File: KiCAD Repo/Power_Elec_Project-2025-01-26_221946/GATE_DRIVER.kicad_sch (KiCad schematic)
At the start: 0 parts

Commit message: lpf design
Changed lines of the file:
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@@
 	(hierarchical_label "VG"
 		(shape output)
-		(at 191.77 29.21 0)
+		(at 190.5 29.21 0)
 		(effects
 			(font

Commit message: gate driver import
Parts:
- added U3: ~, UCC5304DWVR GateDriver_IC:SOIC8_DWV_TEX, symbol UCC5304DWVR:UCC5304DWVR
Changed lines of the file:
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@@
 	(generator_version "8.0")
 	(paper "A4")
+	(wire
+		(pts
+			(xy 93.98 55.88) (xy 93.98 54.61)
+		)
+		(stroke
+			(width 0)
+			(type default)
+		)
+	)
+	(wire
+		(pts
+			(xy 92.71 55.88) (xy 93.98 55.88)
+		)
+		(stroke
+			(width 0)
+			(type default)
+		)
+	)
 	(hierarchical_label "VSW"
 		(shape output)
@@
 	(hierarchical_label "PWM"
 		(shape input)
-		(at 120.65 33.02 0)
-		(effects
-			(font
-				(size 1.27 1.27)
-			)
-			(justify left)
+		(at 92.71 58.42 180)
+		(effects
+			(font
+				(size 1.27 1.27)
+			)
+			(justify right)
 		)
 	)
 	(hierarchical_label "GND"
 		(shape input)
-		(at 120.65 40.64 0)
-		(effects
-			(font
-				(size 1.27 1.27)
-			)
-			(justify left)
+		(at 92.71 60.96 180)
+		(effects
+			(font
+				(size 1.27 1.27)
+			)
+			(justify right)
 		)
 	)
 	(hierarchical_label "5V"
 		(shape input)
-		(at 120.65 26.67 0)
-		(effects
-			(font
-				(size 1.27 1.27)
-			)
-			(justify left)
+		(at 92.71 55.88 180)
+		(effects
+			(font
+				(size 1.27 1.27)
+			)
+			(justify right)
 		)
 	)
@@
 		)
 	)
+	(symbol
+		(lib_id "UCC5304DWVR:UCC5304DWVR")
+		(at 101.6 55.88 0)
+		(unit 1)
+		(exclude_from_sim no)
+		(in_bom yes)
+		(on_board yes)
+		(dnp no)
+		(property "Reference" "U3"
+			(at 110.998 49.276 0)
+			(effects
+				(font
+					(size 1.524 1.524)
+				)
+			)
+		)
+		(property "Value" "~"
+			(at 121.92 48.26 0)
+			(effects
+				(font
+					(size 1.524 1.524)
+				)
+				(hide yes)
+			)
+		)
+		(property "Footprint" "UCC5304DWVR GateDriver_IC:SOIC8_DWV_TEX"
+			(at 101.6 55.88 0)
+			(effects
+				(font
+					(size 1.27 1.27)
+					(italic yes)
+				)
+				(hide yes)
+			)
+		)
+		(property "Datasheet" "https://www.ti.com/lit/ds/symlink/ucc5304.pdf?ts=1739952660041&ref_url=https%253A%252F%252Fwww.mouser.de%252F"
+			(at 101.6 55.88 0)
+			(effects
+				(font
+					(size 1.27 1.27)
+					(italic yes)
+				)
+				(hide yes)
+			)
+		)
+		(property "Description" ""
+			(at 101.6 55.88 0)
+			(effects
+				(font
+					(size 1.27 1.27)
+				)
+				(hide yes)
+			)
+		)
+		(property "Part Number" "UCC5304DWVR"
+			(at 122.428 70.104 0)
+			(effects
+				(font
+					(size 1.27 1.27)
+				)
+			)
+		)
+		(pin "2"
+		)
+		(pin "7"
+		)
+		(pin "5"
+		)
+		(pin "1"
+		)
+		(pin "4"
+		)
+		(pin "6"
+		)
+		(pin "8"
+		)
+		(pin "3"
+		)
+		(instances
+			(project ""
+				(path "/ecd51ed2-b30f-41c1-93fa-3d04786e684e/43f1fb70-bf5d-401c-a26b-88dd12fd13e5"
+					(reference "U3")
+					(unit 1)
+				)
+			)
+		)
+	)
+	(symbol
+		(lib_id "power:+5V")
+		(at 93.98 54.61 0)
+		(unit 1)
+		(exclude_from_sim no)
+		(in_bom yes)
+		(on_board yes)
+		(dnp no)
+		(fields_autoplaced yes)
+		(property "Reference" "#PWR015"
+			(at 93.98 58.42 0)
+			(effects
+				(font
+					(size 1.27 1.27)
+				)
+				(hide yes)
+			)
+		)
+		(property "Value" "+5V"
+			(at 93.98 49.53 0)
+			(effects
+				(font
+					(size 1.27 1.27)
+				)
+			)
+		)
+		(property "Footprint" ""
+			(at 93.98 54.61 0)
+			(effects
+				(font
+					(size 1.27 1.27)
+				)
+				(hide yes)
+			)
+		)
+		(property "Datasheet" ""
+			(at 93.98 54.61 0)
+			(effects
+				(font
+					(size 1.27 1.27)
+				)
+				(hide yes)
+			)
+		)
+		(property "Description" "Power symbol creates a global label with name \"+5V\""
+			(at 93.98 54.61 0)
+			(effects
+				(font
+					(size 1.27 1.27)
+				)
+				(hide yes)
+			)
+		)
+		(pin "1"
+		)
+		(instances
+			(project ""
+				(path "/ecd51ed2-b30f-41c1-93fa-3d04786e684e/43f1fb70-bf5d-401c-a26b-88dd12fd13e5"
+					(reference "#PWR015")
+					(unit 1)
+				)
+			)
+		)
+	)

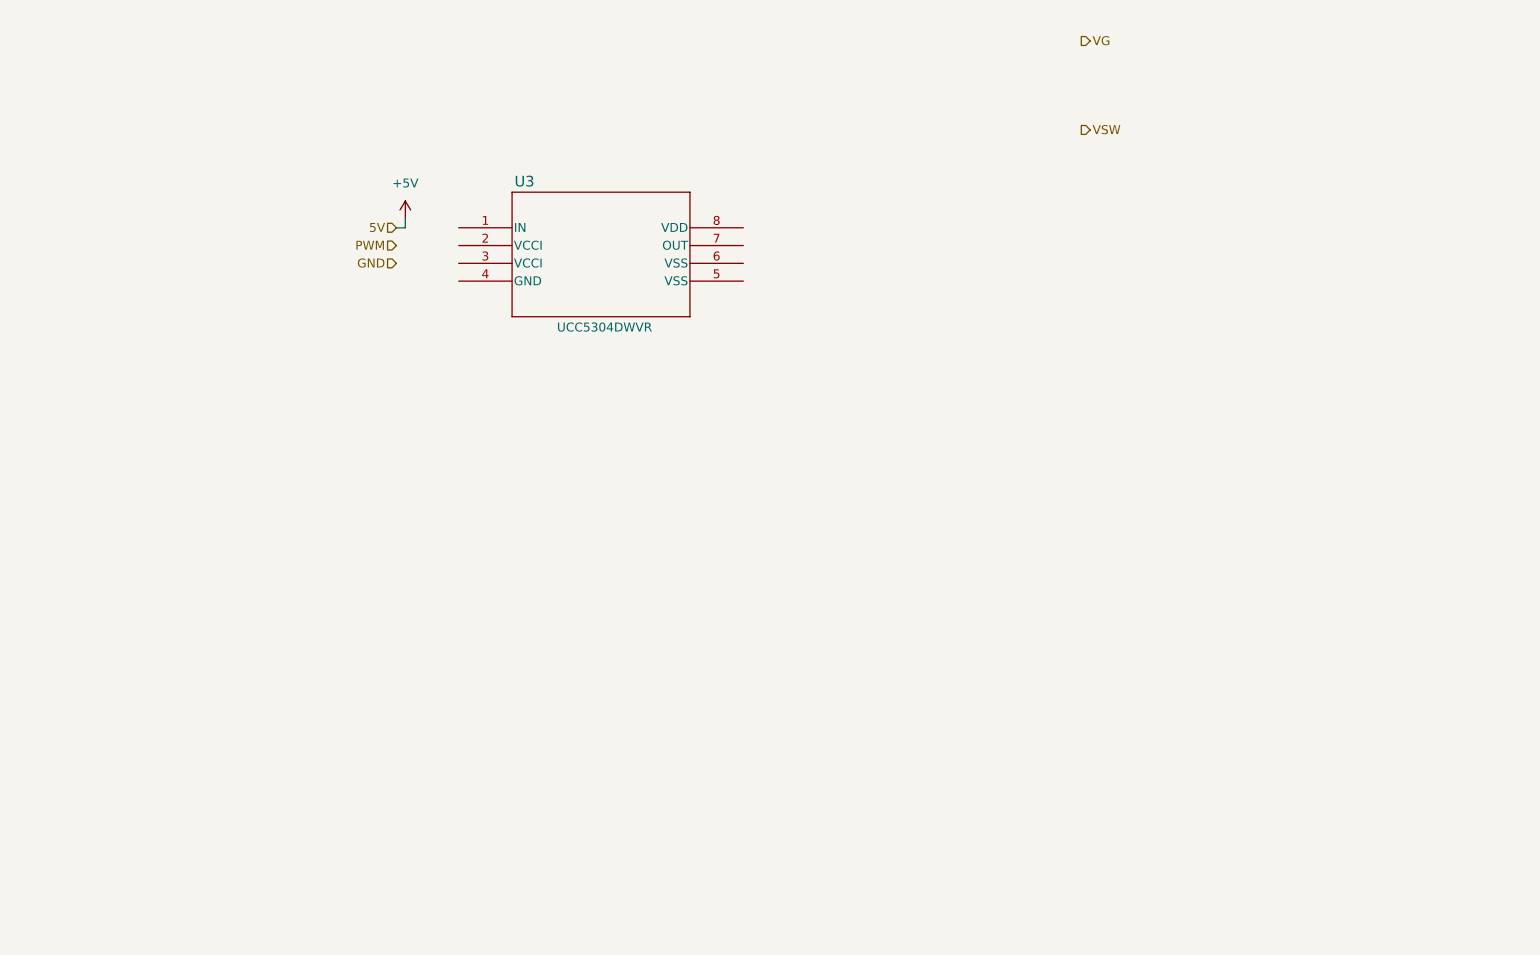
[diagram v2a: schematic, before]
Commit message: PLF and GD circuit
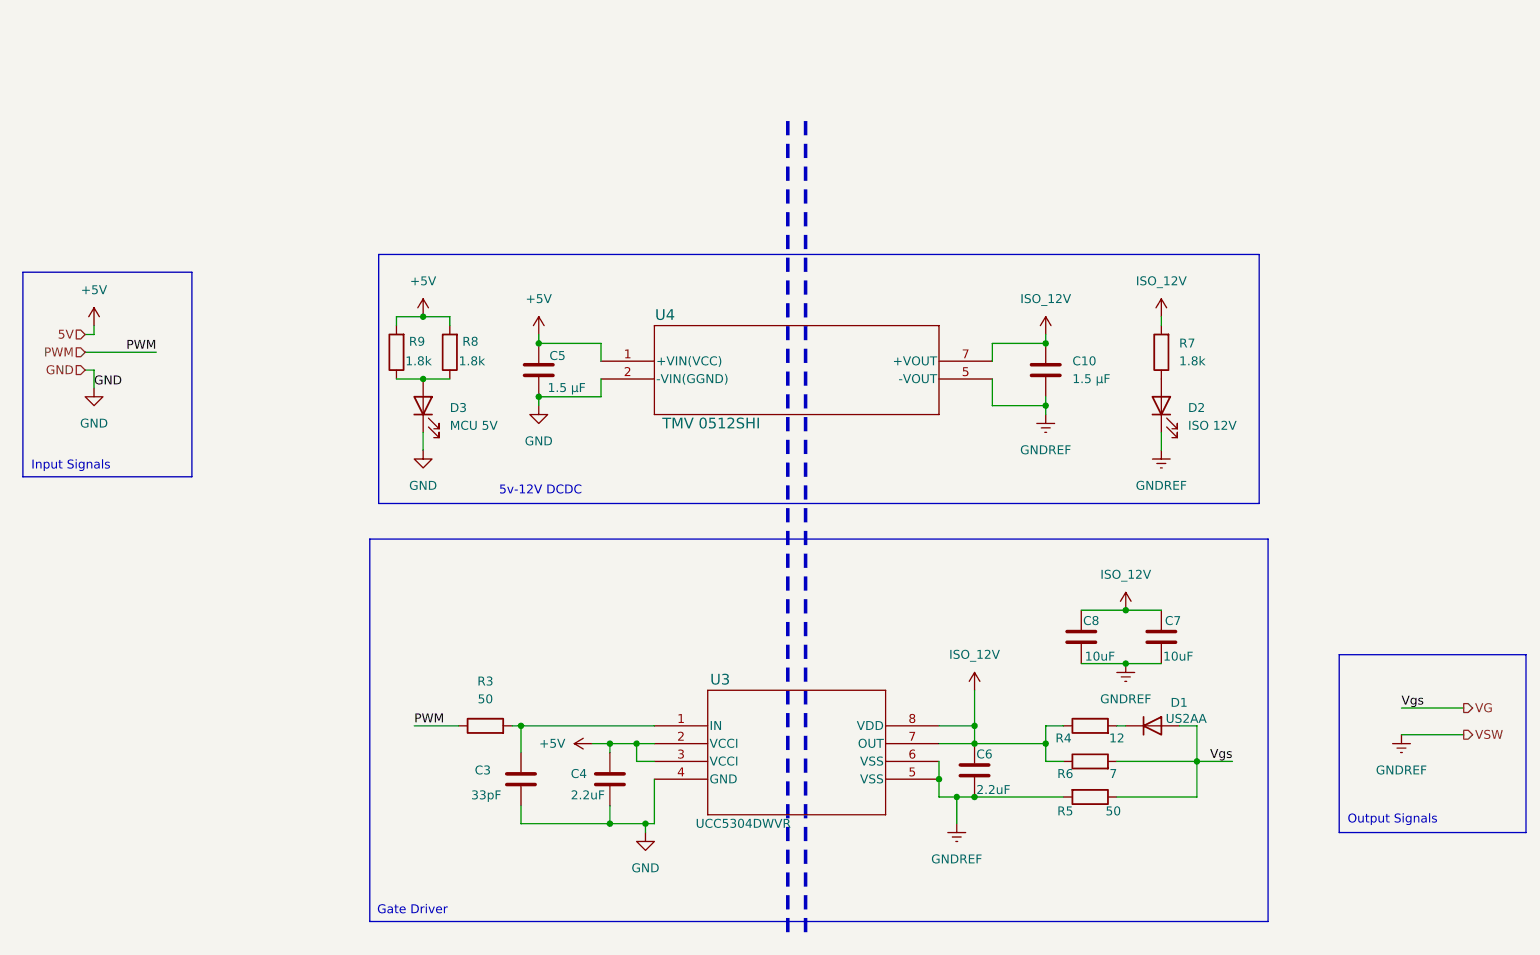
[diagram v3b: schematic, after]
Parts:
- added C10, C5: 1.5 µF, Capacitor_SMD:C_0805_2012Metric, symbol Device:C
- added C3: 33pF, Capacitor_SMD:C_0603_1608Metric, symbol Device:C
- added C4, C6: 2.2uF, Capacitor_SMD:C_0805_2012Metric, symbol Device:C
- added C7, C8: 10uF, Capacitor_SMD:C_0603_1608Metric, symbol Device:C
- added D1: US2AA, Diode_SMD:D_SMA, symbol Diode:US2AA
- added D2: ISO 12V, LED_SMD:LED_0603_1608Metric, symbol Device:LED
- added D3: MCU 5V, LED_SMD:LED_0603_1608Metric, symbol Device:LED
- added R3, R5: 50, Resistor_SMD:R_0603_1608Metric, symbol Device:R
- added R4: 12, Resistor_SMD:R_0805_2012Metric_Pad1.20x1.40mm_HandSolder, symbol Device:R
- added R6: 7, Resistor_SMD:R_0603_1608Metric, symbol Device:R
- added R7, R8, R9: 1.8k, Resistor_SMD:R_0603_1608Metric, symbol Device:R
- added U4: TMV 0512SHI, TMV-HI_SINGLE_TRP, symbol TMV_0512SHI:TMV_0512SHI
- U3: value ~ -> UCC5304DWVR
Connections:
- net +5V: now also U3.2 (VCCI), U3.3 (VCCI), C4.1, C5.1, R8.2, R9.2, U4.1 (+VIN(VCC))
- net GND: now also U3.4 (GND), C3.2, C4.2, C5.2, D3.1 (K), U4.2 (-VIN(GGND))
- net PWM: now also R3.1
- net VG: now also D1.2 (A), R5.1, R6.2
- net at U3.1 (IN): now also C3.1, R3.2
- net GNDREF: now reaches U3.5 (VSS)
- net GNDREF: now also U3.6 (VSS), C10.2, C6.2, C7.2, C8.2, D2.1 (K), R5.2, U4.5 (-VOUT)
- net ISO_12V: now reaches U3.7 (OUT)
- net ISO_12V: now also U3.8 (VDD), C10.1, C6.1, C7.1, C8.1, R4.1, R6.1, R7.2, U4.7 (+VOUT)
- new net: D1.1 (K), R4.2
- new net: D2.2 (A), R7.1
- new net: D3.2 (A), R8.1, R9.1
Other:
- note added: "5v-12V DCDC"
- note added: "Gate Driver"
- note added: "Input Signals"
- note added: "Output Signals"
- company: (none) -> M.Nguyen B.Patel S.Dupuis
- title: (none) -> Gate Driver
- moved on the sheet: U3
